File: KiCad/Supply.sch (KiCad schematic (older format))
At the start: 10 parts, among them J501 6.5V-12V, J502 5V, U501 AZ1117-5.0

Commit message: Schematic Version 4 Some Software Changes
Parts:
- C501, J501, U501: Assembly (none) -> DNP
- D502: footprint LEDs:LED_0805 -> LEDs:LED_D3.0mm
- R501: value 430 -> 2k2
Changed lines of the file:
@@
 EESchema Schematic File Version 3
+LIBS:ledbox-rescue
 LIBS:power
 LIBS:device
@@
 LIBS:contrib
 LIBS:ledbox-newsymbols
+LIBS:74xxLVCxG
+LIBS:analog_devices
+LIBS:boards
+LIBS:bridge_rectifier
+LIBS:caf
+LIBS:cirrus logic
+LIBS:eeprom
+LIBS:ft232rl
+LIBS:linear_technology
+LIBS:micrel
+LIBS:NXP Semiconductor
+LIBS:SigmaDSP
+LIBS:texas_instruments
+LIBS:tl431
+LIBS:toslink
+LIBS:worldsemi
+LIBS:ac-dc
+LIBS:Altera
+LIBS:Battery_Management
+LIBS:bbd
+LIBS:Bosch
+LIBS:brooktre
+LIBS:Connector
+LIBS:dc-dc
+LIBS:Decawave
+LIBS:Diode
+LIBS:Display
+LIBS:driver_gate
+LIBS:DSP_Microchip_DSPIC33
+LIBS:elec-unifil
+LIBS:ESD_Protection
+LIBS:Espressif
+LIBS:FPGA_Actel
+LIBS:ftdi
+LIBS:gennum
+LIBS:Graphic
+LIBS:hc11
+LIBS:infineon
+LIBS:intersil
+LIBS:ir
+LIBS:Lattice
+LIBS:LED
+LIBS:LEM
+LIBS:Logic_74xgxx
+LIBS:Logic_74xx
+LIBS:Logic_CMOS_4000
+LIBS:Logic_CMOS_IEEE
+LIBS:logic_programmable
+LIBS:Logic_TTL_IEEE
+LIBS:maxim
+LIBS:MCU_Microchip_PIC10
+LIBS:MCU_Microchip_PIC12
+LIBS:MCU_Microchip_PIC16
+LIBS:MCU_Microchip_PIC18
+LIBS:MCU_Microchip_PIC24
+LIBS:MCU_Microchip_PIC32
+LIBS:MCU_NXP_Kinetis
+LIBS:MCU_NXP_LPC
+LIBS:MCU_NXP_S08
+LIBS:MCU_Parallax
+LIBS:MCU_ST_STM8
+LIBS:MCU_ST_STM32
+LIBS:MCU_Texas_MSP430
+LIBS:Mechanical
+LIBS:modules
+LIBS:motor_drivers
+LIBS:Motor
+LIBS:nordicsemi
+LIBS:nxp
+LIBS:onsemi
+LIBS:Oscillators
+LIBS:Power_Management
+LIBS:powerint
+LIBS:pspice
+LIBS:references
+LIBS:Relay
+LIBS:RF_Bluetooth
+LIBS:rfcom
+LIBS:RFSolutions
+LIBS:Sensor_Current
+LIBS:Sensor_Humidity
+LIBS:sensors
+LIBS:silabs
+LIBS:supertex
+LIBS:Switch
+LIBS:Transformer
+LIBS:Transistor
+LIBS:triac_thyristor
+LIBS:Valve
+LIBS:video
+LIBS:wiznet
+LIBS:Worldsemi
+LIBS:Xicor
+LIBS:xilinx-artix7
+LIBS:xilinx-kintex7
+LIBS:xilinx-spartan6
+LIBS:xilinx-virtex5
+LIBS:xilinx-virtex6
+LIBS:xilinx-virtex7
+LIBS:zetex
+LIBS:Zilog
 LIBS:ledbox-cache
 EELAYER 26 0
@@
 $Descr A4 11693 8268
 encoding utf-8
-Sheet 5 5
+Sheet 4 5
 Title ""
 Date ""
@@
 F 2 "Capacitors_THT:CP_Radial_D5.0mm_P2.00mm" H 5138 4100 50  0001 C CNN
 F 3 "" H 5100 4250 50  0001 C CNN
+F 4 "DNP" H 5100 4250 60  0001 C CNN "Assembly"
 	1    5100 4250
 	1    0    0    -1
@@
 F 2 "Connectors_Terminal_Blocks:TerminalBlock_Pheonix_MKDS1.5-2pol" H 4000 3800 50  0001 C CNN
 F 3 "" H 4000 3800 50  0001 C CNN
+F 4 "DNP" H 4000 3800 60  0001 C CNN "Assembly"
 	1    4000 3800
 	-1   0    0    -1
 $EndComp
 $Comp
-L +12V #PWR501
+L +12V #PWR0501
 U 1 1 59DBA13C
 P 4300 3700
-F 0 "#PWR501" H 4300 3550 50  0001 C CNN
+F 0 "#PWR0501" H 4300 3550 50  0001 C CNN
 F 1 "+12V" H 4300 3840 50  0000 C CNN
 F 2 "" H 4300 3700 50  0001 C CNN
@@
 $EndComp
 $Comp
-L GND #PWR502
+L GND #PWR0502
 U 1 1 59DBA1A9
 P 4300 4000
-F 0 "#PWR502" H 4300 3750 50  0001 C CNN
+F 0 "#PWR0502" H 4300 3750 50  0001 C CNN
 F 1 "GND" H 4300 3850 50  0000 C CNN
 F 2 "" H 4300 4000 50  0001 C CNN
@@
 $EndComp
 $Comp
-L GND #PWR504
+L GND #PWR0504
 U 1 1 59DBA33D
 P 4300 4700
-F 0 "#PWR504" H 4300 4450 50  0001 C CNN
+F 0 "#PWR0504" H 4300 4450 50  0001 C CNN
 F 1 "GND" H 4300 4550 50  0000 C CNN
 F 2 "" H 4300 4700 50  0001 C CNN
@@
 $EndComp
 $Comp
-L +5V #PWR503
+L +5V #PWR0503
 U 1 1 59DBA35E
 P 4300 4400
-F 0 "#PWR503" H 4300 4250 50  0001 C CNN
+F 0 "#PWR0503" H 4300 4250 50  0001 C CNN
 F 1 "+5V" H 4300 4540 50  0000 C CNN
 F 2 "" H 4300 4400 50  0001 C CNN
@@
 F 2 "TO_SOT_Packages_SMD:SOT-223-3Lead_TabPin2" H 5800 4250 50  0001 C CIN
 F 3 "" H 5800 4000 50  0001 C CNN
+F 4 "DNP" H 5800 4000 60  0001 C CNN "Assembly"
 	1    5800 4000
 	1    0    0    -1
@@
 $EndComp
 $Comp
-L +12V #PWR505
+L +12V #PWR0505
 U 1 1 59DBA74B
 P 5100 3900
-F 0 "#PWR505" H 5100 3750 50  0001 C CNN
+F 0 "#PWR0505" H 5100 3750 50  0001 C CNN
 F 1 "+12V" H 5100 4040 50  0000 C CNN
 F 2 "" H 5100 3900 50  0001 C CNN
@@
 $EndComp
 $Comp
-L GND #PWR506
+L GND #PWR0506
 U 1 1 59DBA861
 P 5800 4600
-F 0 "#PWR506" H 5800 4350 50  0001 C CNN
+F 0 "#PWR0506" H 5800 4350 50  0001 C CNN
 F 1 "GND" H 5800 4450 50  0000 C CNN
 F 2 "" H 5800 4600 50  0001 C CNN
@@
 $EndComp
 $Comp
-L +5V #PWR507
+L +5V #PWR0507
 U 1 1 59DBAA1E
 P 6500 3900
-F 0 "#PWR507" H 6500 3750 50  0001 C CNN
+F 0 "#PWR0507" H 6500 3750 50  0001 C CNN
 F 1 "+5V" H 6500 4040 50  0000 C CNN
 F 2 "" H 6500 3900 50  0001 C CNN
@@
 F 0 "D502" H 7100 4150 50  0000 C CNN
 F 1 "LED2" H 7100 3950 50  0000 C CNN
-F 2 "LEDs:LED_0805" H 7100 4050 50  0001 C CNN
+F 2 "LEDs:LED_D3.0mm" H 7100 4050 50  0001 C CNN
 F 3 "" H 7100 4050 50  0001 C CNN
 	1    7100 4050
@@
 P 7100 4450
 F 0 "R501" V 7180 4450 50  0000 C CNN
-F 1 "430" V 7100 4450 50  0000 C CNN
+F 1 "2k2" V 7100 4450 50  0000 C CNN
 F 2 "Resistors_SMD:R_0805" V 7030 4450 50  0001 C CNN
 F 3 "" H 7100 4450 50  0001 C CNN
@@
 $EndComp
 $Comp
-L +5V #PWR508
+L +5V #PWR0508
 U 1 1 59E32AF0
 P 7100 3800
-F 0 "#PWR508" H 7100 3650 50  0001 C CNN
+F 0 "#PWR0508" H 7100 3650 50  0001 C CNN
 F 1 "+5V" H 7100 3940 50  0000 C CNN
 F 2 "" H 7100 3800 50  0001 C CNN
@@
 	7100 4200 7100 4300
 $Comp
-L GND #PWR509
+L GND #PWR0509
 U 1 1 59E32B42
 P 7100 4700
-F 0 "#PWR509" H 7100 4450 50  0001 C CNN
+F 0 "#PWR0509" H 7100 4450 50  0001 C CNN
 F 1 "GND" H 7100 4550 50  0000 C CNN
 F 2 "" H 7100 4700 50  0001 C CNN

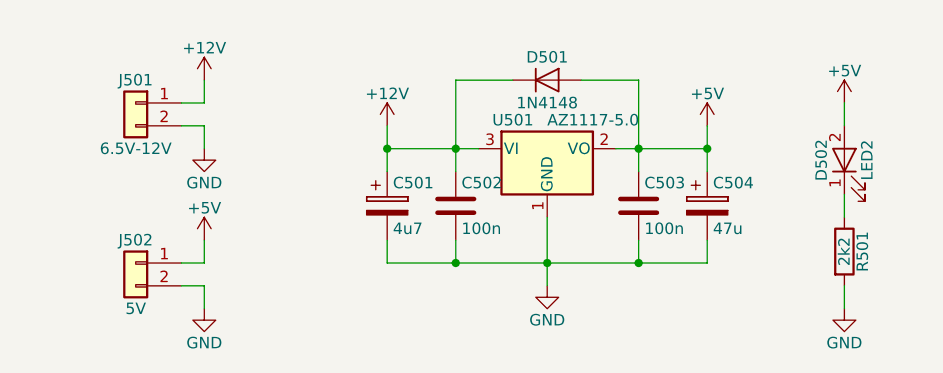
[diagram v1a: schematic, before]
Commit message: Changes to V4 Schematic, new Board design
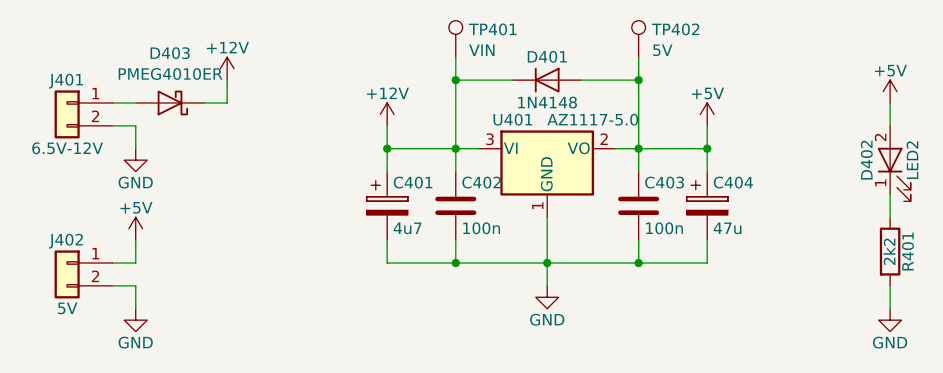
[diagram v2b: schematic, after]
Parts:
- added D403: PMEG4010ER, Diodes_SMD:D_SOD-123, symbol D_Schottky
- added TP401: VIN, Test:TEST_10, symbol Test_Point
- added TP402: 5V, Test:TEST_10, symbol Test_Point
- J401: renamed from J501; footprint Connectors_Terminal_Blocks:TerminalBlock_Pheonix_MKDS1.5-2pol -> TerminalBlock_MetzConnect:TerminalBlock_MetzConnect_Type055_RT01502HDWU_Pitch5.00mm
- J402: renamed from J502; footprint Connectors_Terminal_Blocks:TerminalBlock_Pheonix_MKDS1.5-2pol -> TerminalBlock_MetzConnect:TerminalBlock_MetzConnect_Type055_RT01502HDWU_Pitch5.00mm
- U401: renamed from U501; footprint TO_SOT_Packages_SMD:SOT-223-3Lead_TabPin2 -> TO_SOT_Packages_SMD:SOT-223-3_TabPin2
- renumbered C501 to C401, C502 to C402, C503 to C403, C504 to C404, D501 to D401, D502 to D402, R501 to R401
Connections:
- net +12V: now also D403.1 (K), TP401.1; no longer J401.1 (Pin_1)
- net +5V: now also TP402.1
- new net: D403.2 (A), J401.1 (Pin_1)
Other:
- moved on the sheet: D402, J401, J402, R401
